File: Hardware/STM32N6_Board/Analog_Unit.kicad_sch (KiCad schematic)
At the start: 1 part

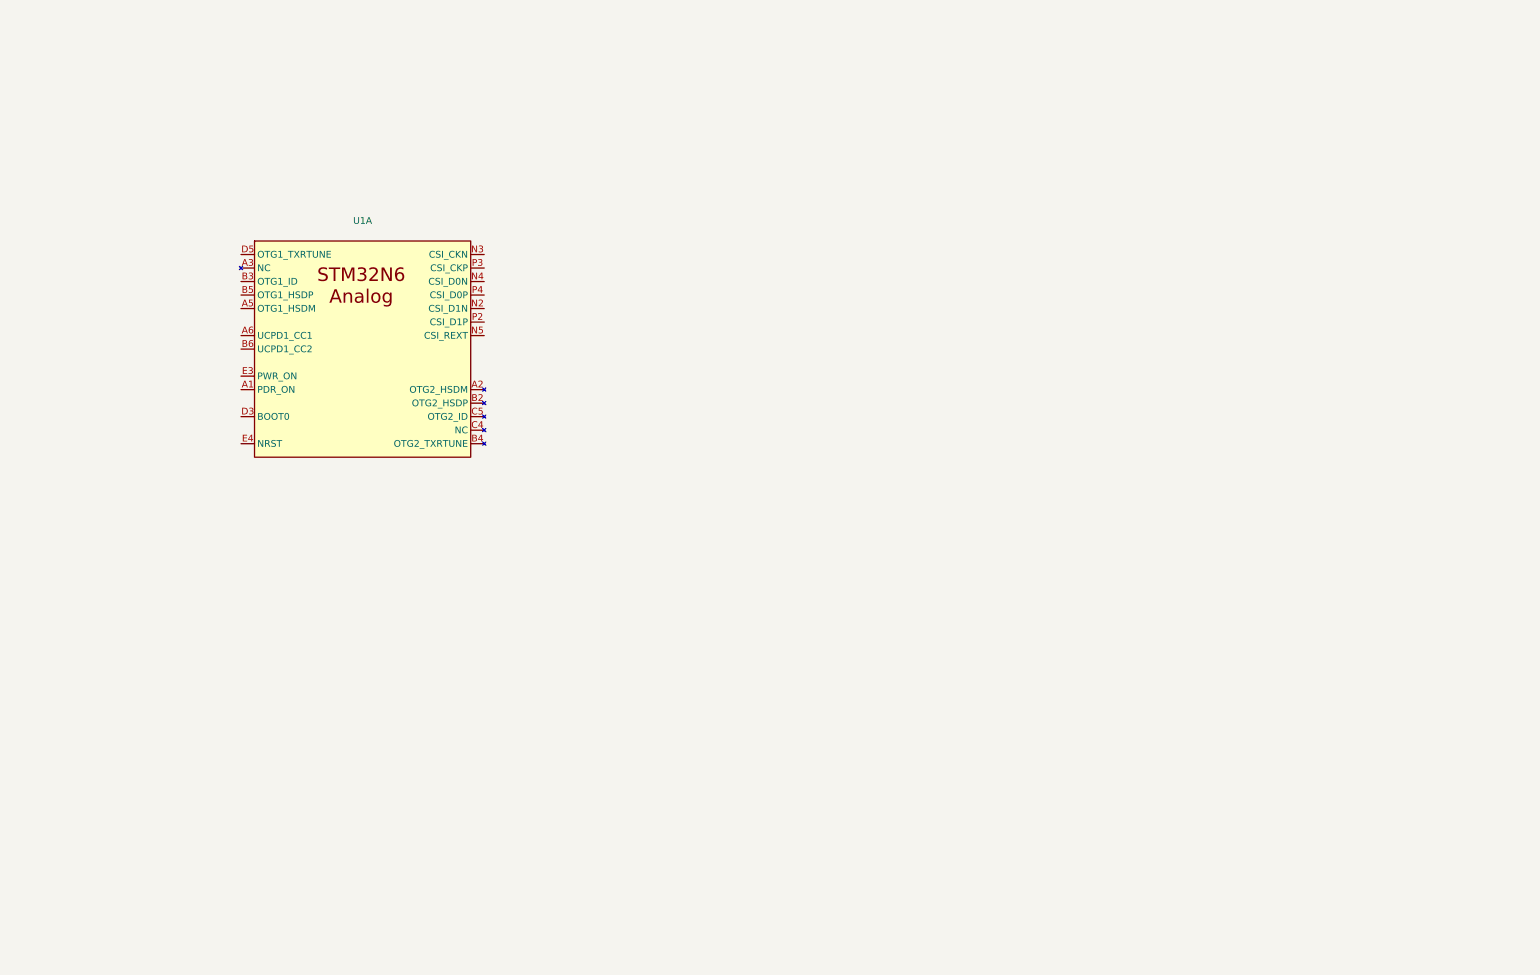
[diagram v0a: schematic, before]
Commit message: Completed wiring of the Analog unit.
- CSI and USB buses are created, yet to be connected with connectors
- Next will be pin selection, and drawing in FMC SDRAM
- Then will be routing GPIOs as buses, and connecting with connectors
- Finally, board layout.
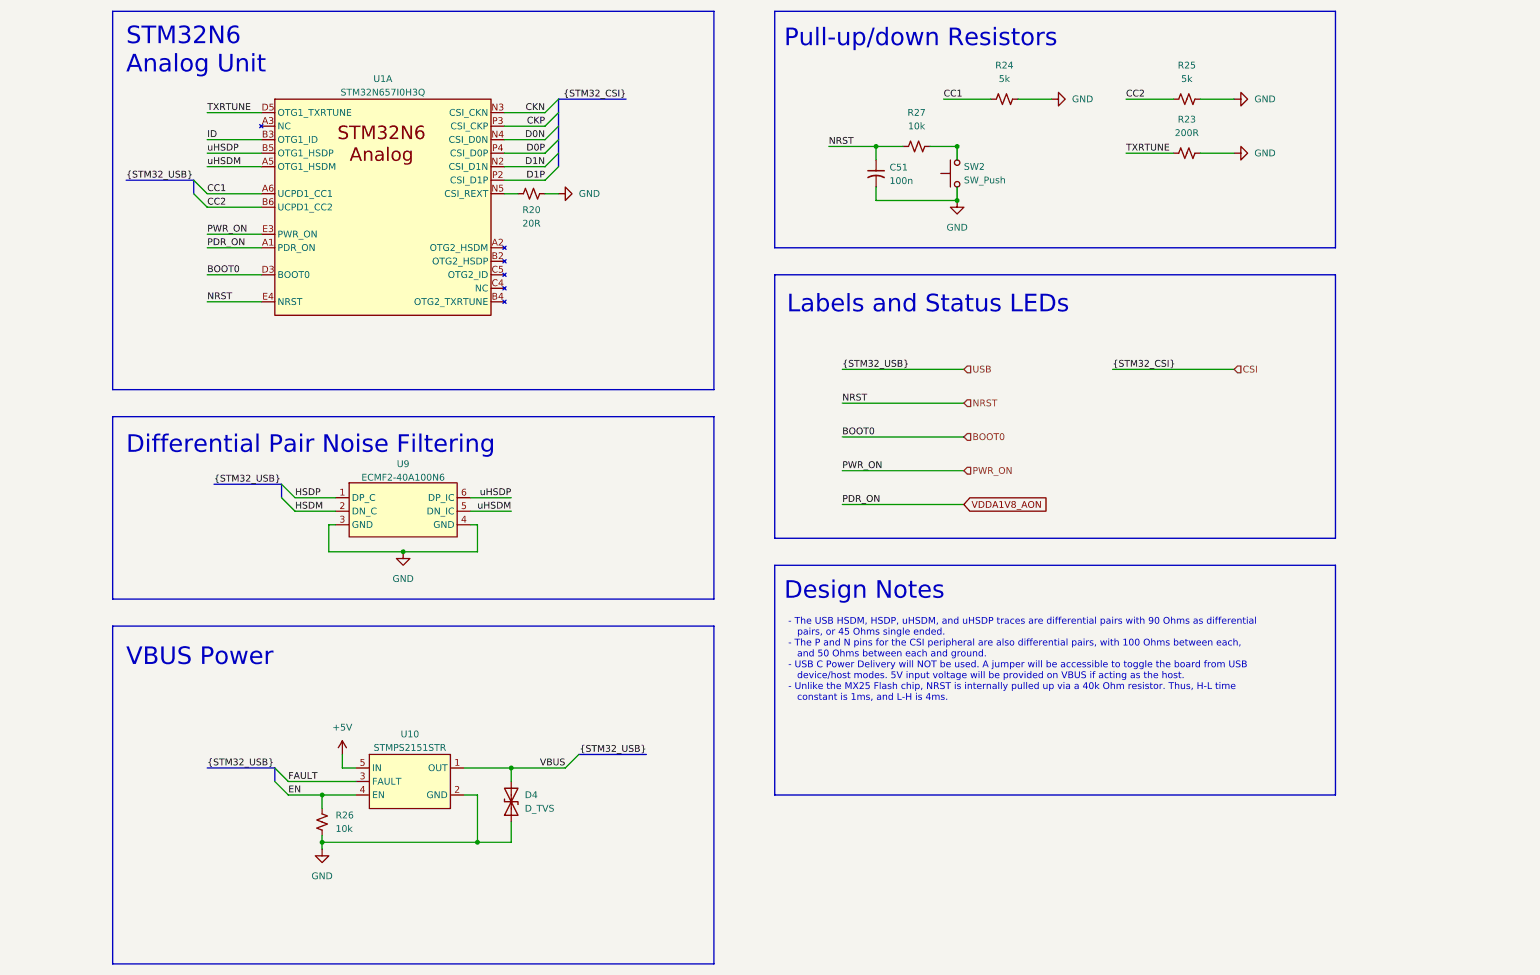
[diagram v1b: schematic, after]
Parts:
- added C51: 100n, symbol Device:C_Small_US
- added D4: D_TVS, symbol Device:D_TVS
- added R20: 20R, symbol Device:R_Small_US
- added R23: 200R, symbol Device:R_Small_US
- added R24, R25: 5k, symbol Device:R_Small_US
- added R26, R27: 10k, symbol Device:R_Small_US
- added SW2: SW_Push, symbol Switch:SW_Push
- added U10: STMPS2151STR, symbol STM32N6_Symbols:STMPS2151STR
- added U9: ECMF2-40A100N6, symbol STM32N6_Symbols:ECMF2-40A100N6
- U1: value ~ -> STM32N657I0H3Q
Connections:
- net VDDA1V8_AON: now reaches U1.A1 (PDR_ON)
- net uHSDM: now reaches U1.A5 (OTG1_HSDM)
- net uHSDM: now also U9.5 (DN_IC)
- net CC1: now reaches U1.A6 (UCPD1_CC1)
- net CC1: now also R24.1
- net ID: now reaches U1.B3 (OTG1_ID)
- net uHSDP: now reaches U1.B5 (OTG1_HSDP)
- net uHSDP: now also U9.6 (DP_IC)
- net CC2: now reaches U1.B6 (UCPD1_CC2)
- net CC2: now also R25.1
- net BOOT0: now reaches U1.D3 (BOOT0)
- net TXRTUNE: now reaches U1.D5 (OTG1_TXRTUNE)
- net TXRTUNE: now also R23.1
- net PWR_ON: now reaches U1.E3 (PWR_ON)
- net NRST: now reaches U1.E4 (NRST)
- net NRST: now also C51.1, R27.1
- net D1N: now reaches U1.N2 (CSI_D1N)
- net CKN: now reaches U1.N3 (CSI_CKN)
- net D0N: now reaches U1.N4 (CSI_D0N)
- net at U1.N5 (CSI_REXT): now also R20.1
- net D1P: now reaches U1.P2 (CSI_D1P)
- net CKP: now reaches U1.P3 (CSI_CKP)
- net D0P: now reaches U1.P4 (CSI_D0P)
- new net: R27.2, SW2.2
- new net +5V: U10.5 (IN)
- new net EN: R26.2, U10.4 (EN)
- new net FAULT: U10.3 (FAULT)
- new net GND: C51.2, D4.1 (A1), R20.2, R23.2, R24.2, R25.2, R26.1, SW2.1, U10.2 (GND), U9.3 (GND), U9.4 (GND)
- new net HSDM: U9.2 (DN_C)
- new net HSDP: U9.1 (DP_C)
- new net VBUS: D4.2 (A2), U10.1 (OUT)
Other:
- note added: "- The USB HSDM, HSDP, uHSDM, and uHSDP traces are differential pairs with 90 Ohms as differential pairs, or 45 Ohms single ended. - The P and N pins for the CSI peripheral are also differential pairs, with 100 Ohms between each, and 50 Ohms between each and ground. - USB C Power Delivery will NOT be used. A jumper will be accessible to toggle the board from USB device/host modes. 5V input voltage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"
- note added: "Design Notes"
- note added: "Differential Pair Noise Filtering"
- note added: "Labels and Status LEDs"
- note added: "Pull-up/down Resistors"
- note added: "STM32N6 Analog Unit"
- note added: "VBUS Power"
- title: (none) -> SolarVision Mower - STM32N6 Board - Analog Unit
- moved on the sheet: U1A

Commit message: Added and Updated some stuff
- Added layout guide for the IS42 SDRAM chip
- Modified reset pins wiring (now only on one reset button)
- Added design notes in docs/STM32N6/DesignNotes.md
- Updated PROGRESS.md
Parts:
- added D5: D, symbol Device:D
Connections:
- net +5V: now also D5.1 (K)
- net NRST: now also R27.2, SW2.2; no longer C51.1, R27.1
- net VBUS: now also D5.2 (A)
- new net: C51.1, R27.1
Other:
- note added: "- The USB HSDM, HSDP, uHSDM, and uHSDP traces are differential pairs with 90 Ohms as differential pairs, or 45 Ohms single ended. - The P and N pins for the CSI peripheral are also differential pairs, with 100 Ohms between each, and 50 Ohms between each and ground. - USB C Power Delivery will be used, but may be disabled by unsoldering D5. A jumper will be accessible to toggle the board from USB 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"
- note removed: "- The USB HSDM, HSDP, uHSDM, and uHSDP traces are differential pairs with 90 Ohms as differential pairs, or 45 Ohms single ended. - The P and N pins for the CSI peripheral are also differential pairs, with 100 Ohms between each, and 50 Ohms between each and ground. - USB C Power Delivery will NOT be used. A jumper will be accessible to toggle the board from USB device/host modes. 5V input voltage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"
- moved on the sheet: C51, R27, SW2

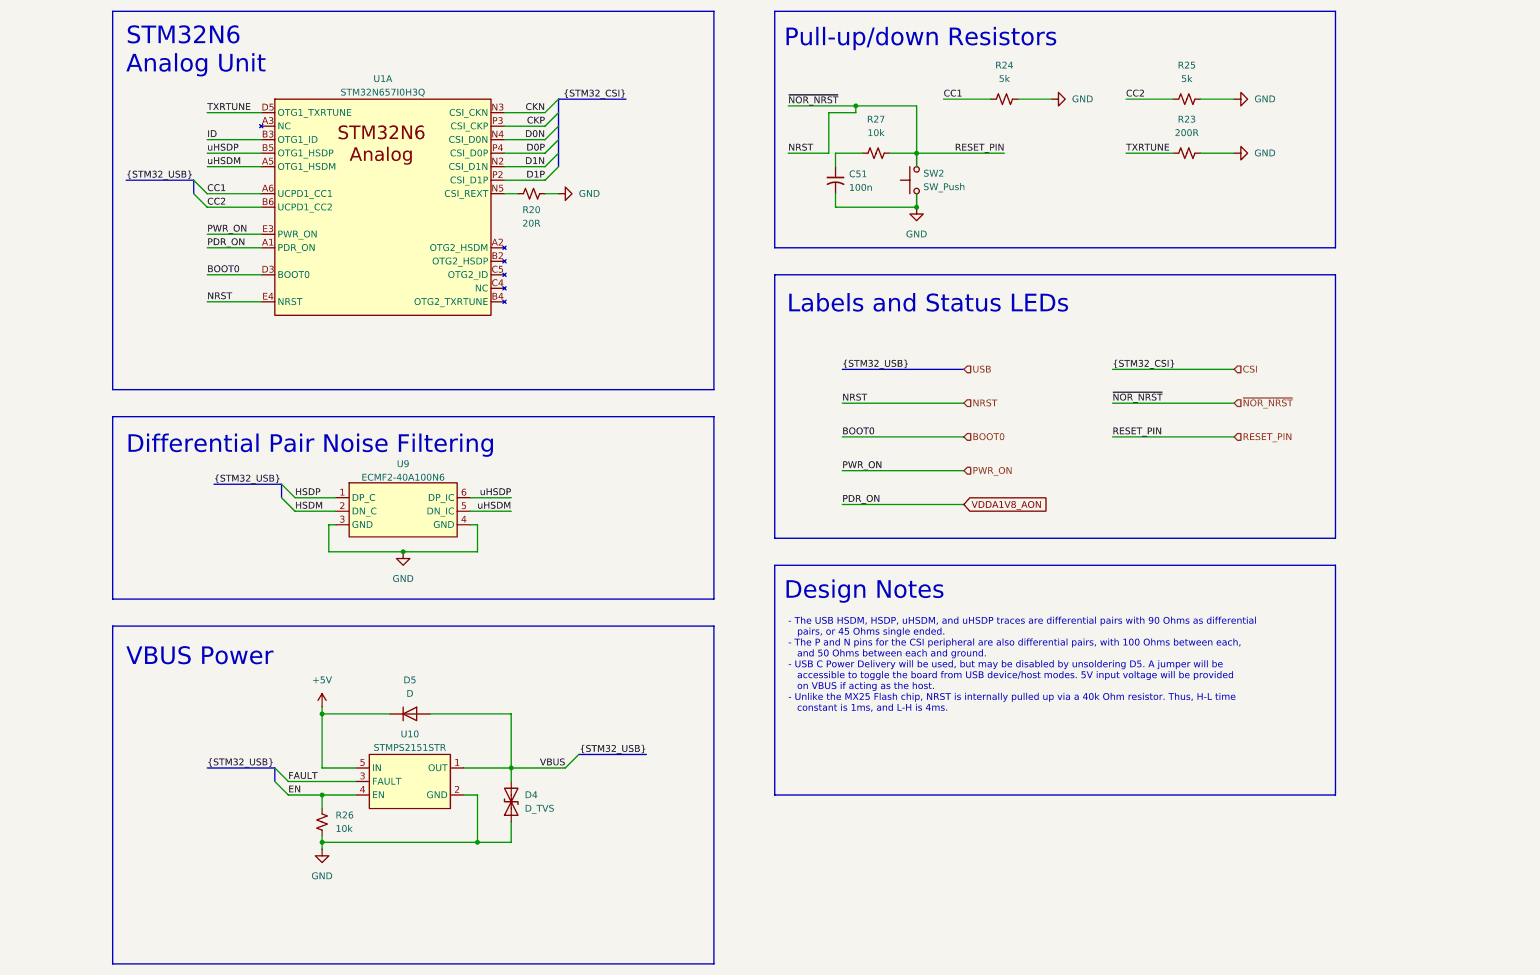
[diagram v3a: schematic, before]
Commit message: Completed the schematic.
- The schematic is complete.
- ERC checker, footprint assignment, and PCB board design left
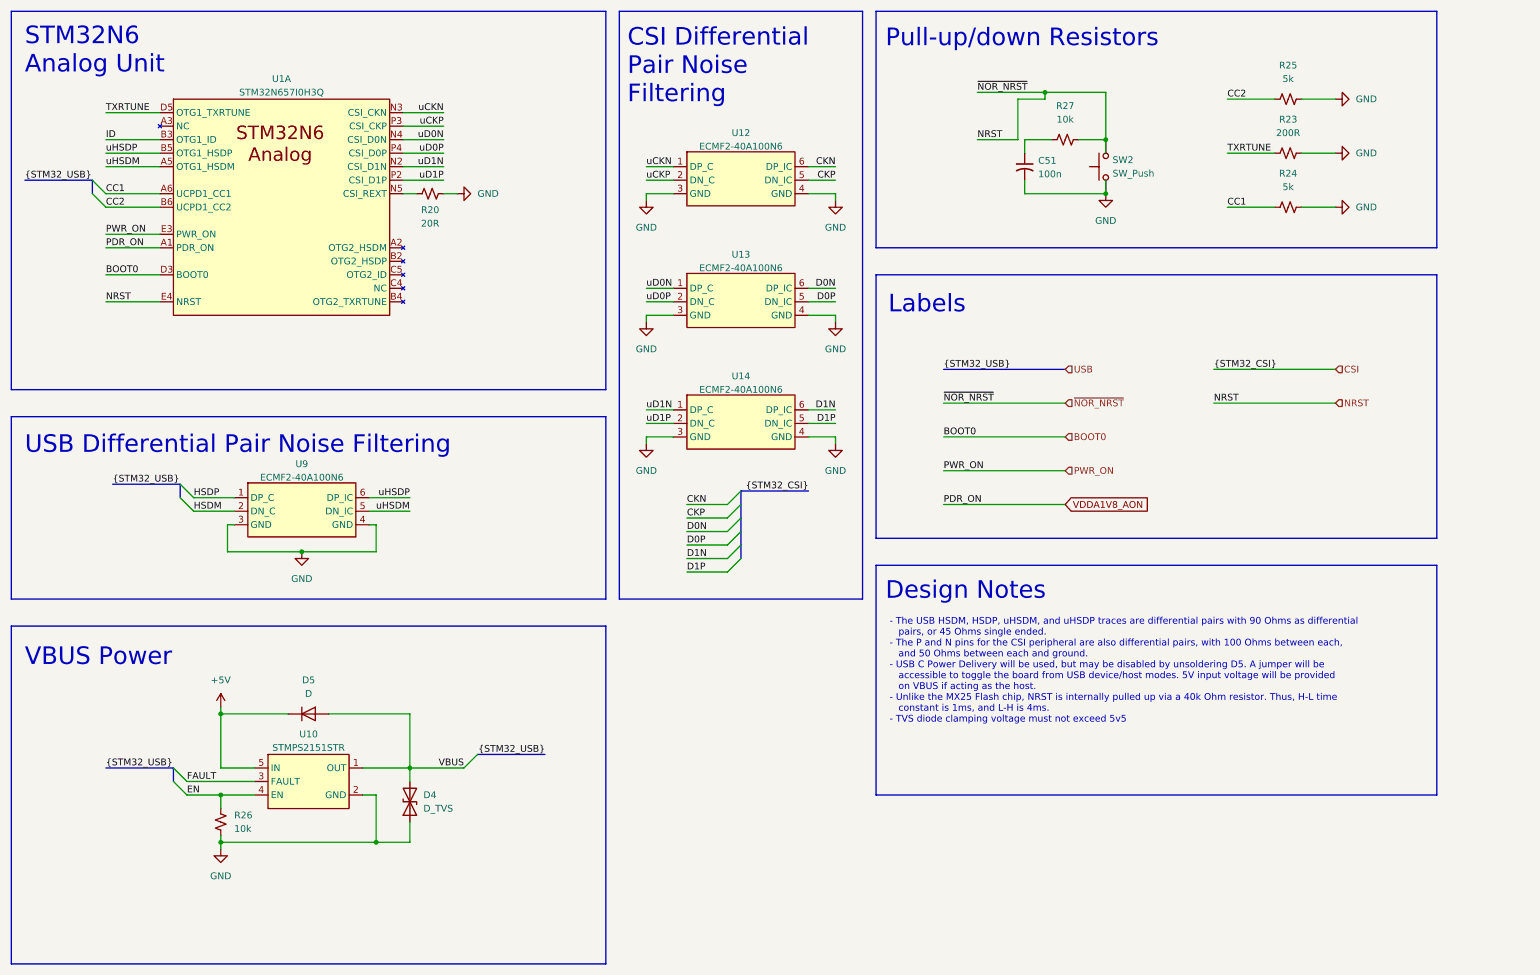
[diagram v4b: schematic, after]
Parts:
- added U12, U13, U14: ECMF2-40A100N6, symbol STM32N6_Symbols:ECMF2-40A100N6
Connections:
- net CKN: now also U12.6 (DP_IC); no longer U1.N3 (CSI_CKN)
- net CKP: now also U12.5 (DN_IC); no longer U1.P3 (CSI_CKP)
- net D0N: now also U13.6 (DP_IC); no longer U1.N4 (CSI_D0N)
- net D0P: now also U13.5 (DN_IC); no longer U1.P4 (CSI_D0P)
- net D1N: now also U14.6 (DP_IC); no longer U1.N2 (CSI_D1N)
- net D1P: now also U14.5 (DN_IC); no longer U1.P2 (CSI_D1P)
- net GND: now also U12.3 (GND), U12.4 (GND), U13.3 (GND), U13.4 (GND), U14.3 (GND), U14.4 (GND)
- new net uCKN: U1.N3 (CSI_CKN), U12.1 (DP_C)
- new net uCKP: U1.P3 (CSI_CKP), U12.2 (DN_C)
- new net uD0N: U1.N4 (CSI_D0N), U13.1 (DP_C)
- new net uD0P: U1.P4 (CSI_D0P), U13.2 (DN_C)
- new net uD1N: U1.N2 (CSI_D1N), U14.1 (DP_C)
- new net uD1P: U1.P2 (CSI_D1P), U14.2 (DN_C)
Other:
- note added: "CSI Differential Pair Noise Filtering"
- note added: "Labels"
- note added: "USB Differential Pair Noise Filtering"
- note removed: "Differential Pair Noise Filtering"
- note removed: "Labels and Status LEDs"
- moved on the sheet: C51, D4, D5, R20, R23, R24, R25, R26, R27, SW2, U10, U1A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

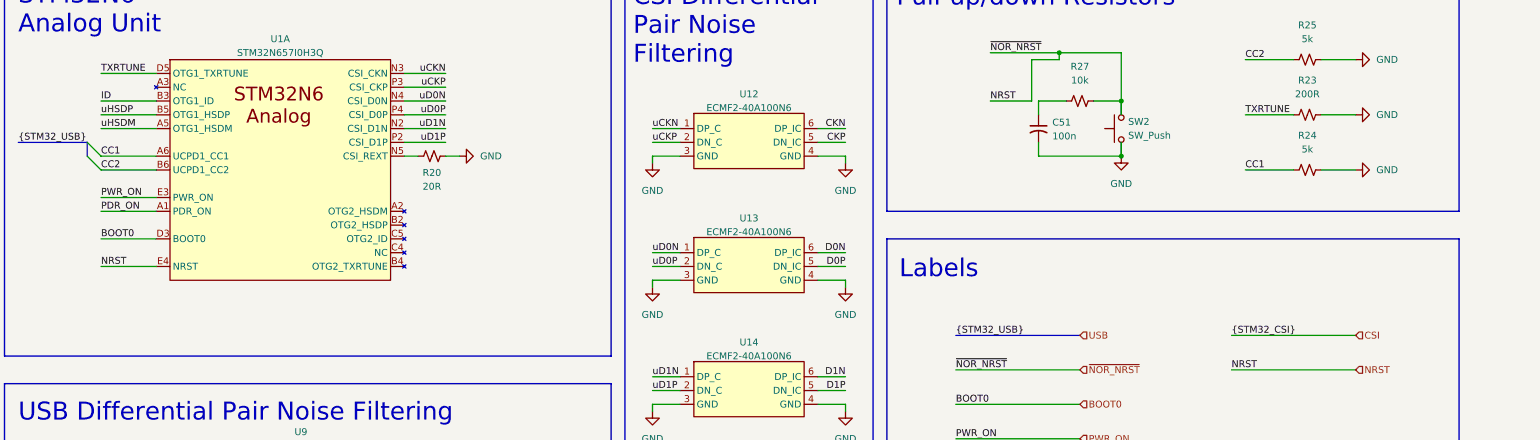
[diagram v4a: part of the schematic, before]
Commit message: Made fixes to remove ERC errors
- 1 remaining error, but > 100 warnings D:
- The remaining error is a bug within KiCAD I believe
- Next is footprint assignment
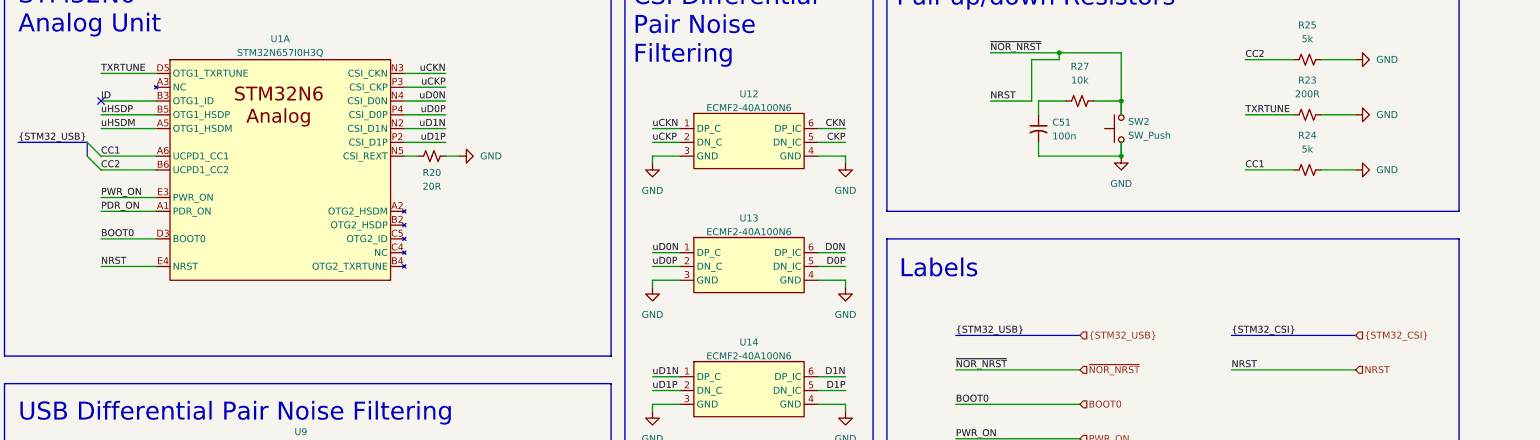
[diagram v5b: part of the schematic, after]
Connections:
- no-connect marks 0 -> 1
